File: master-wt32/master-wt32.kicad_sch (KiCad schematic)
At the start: 4 parts, among them J1 Conn_01x06_Male, J2 Conn_01x06_Male, J3 Conn_01x06_Female, J4 Conn_01x06_Female

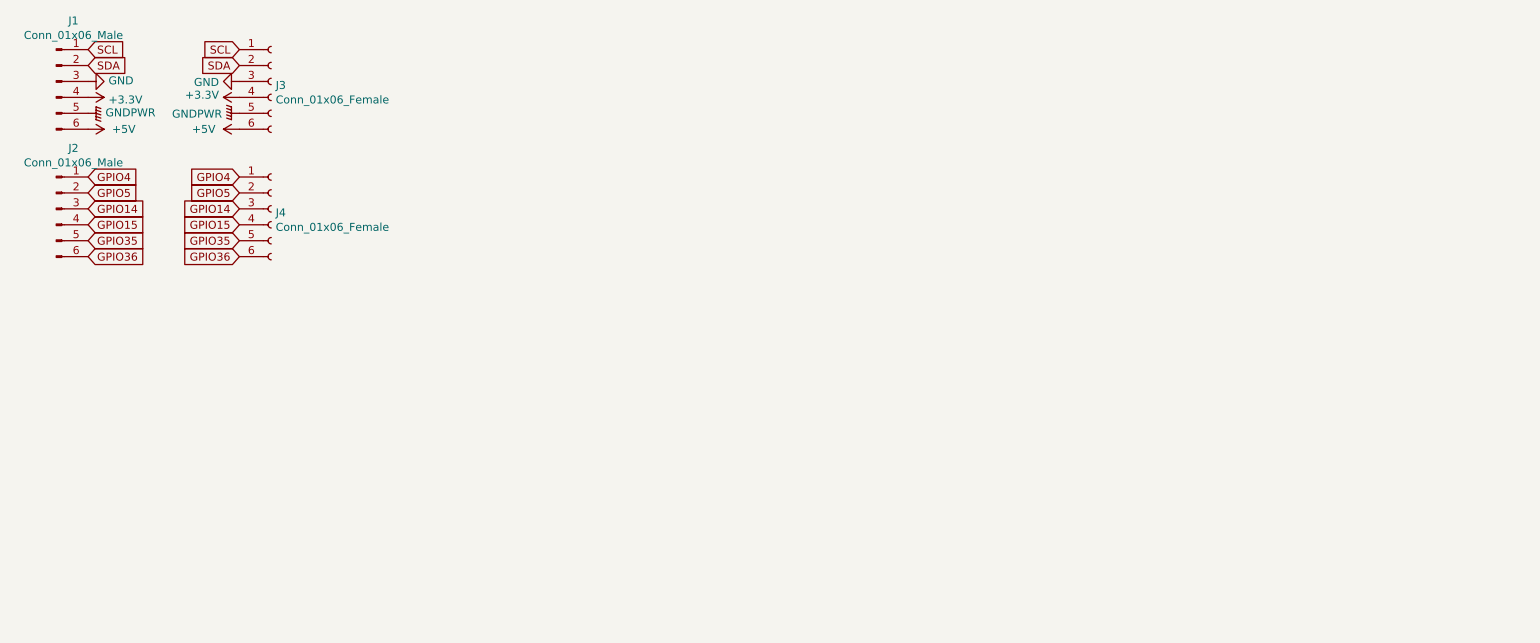
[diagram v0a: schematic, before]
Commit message: add components to master-wt32
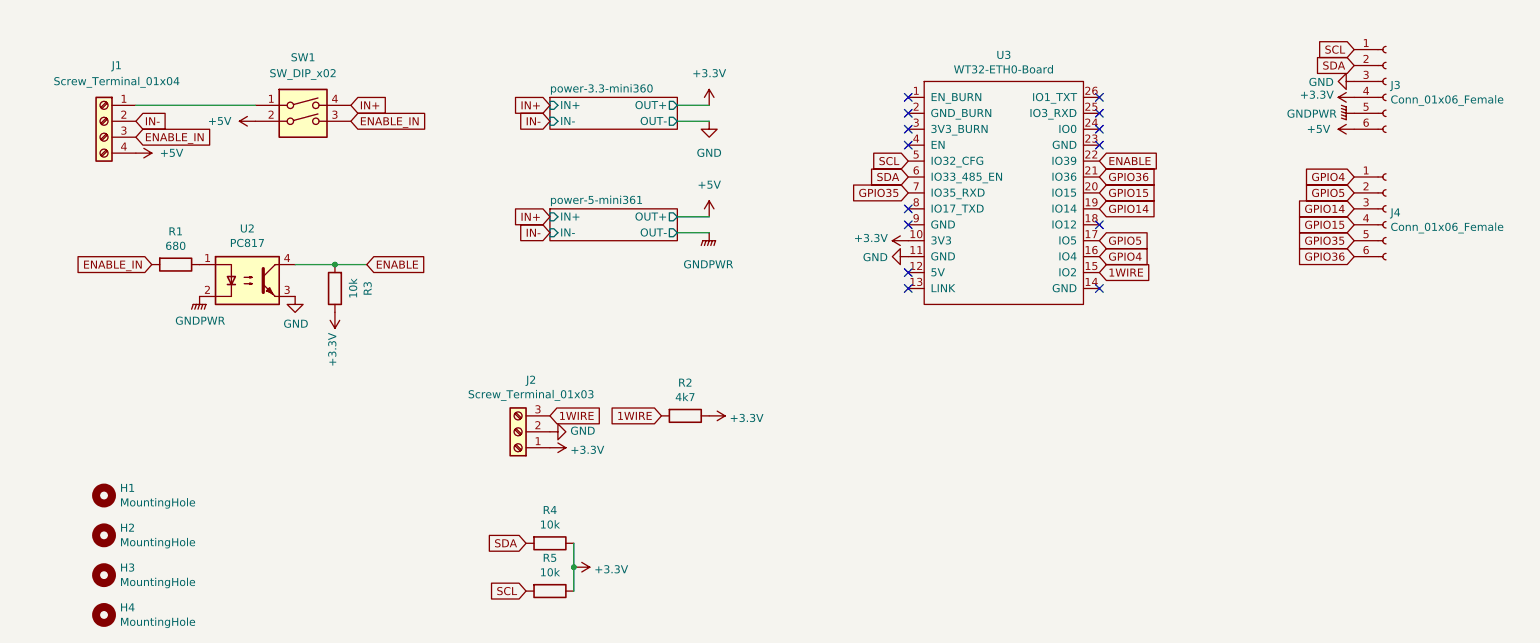
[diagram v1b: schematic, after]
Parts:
- removed J1, J2: Conn_01x06_Male, Connector_PinHeader_2.54mm:PinHeader_1x06_P2.54mm_Horizontal, symbol Connector:Conn_01x06_Male
- added H1, H2, H3, H4: MountingHole, MountingHole:MountingHole_3.2mm_M3, symbol Mechanical:MountingHole
- added J1: Screw_Terminal_01x04, TerminalBlock:TerminalBlock_bornier-4_P5.08mm, symbol Connector:Screw_Terminal_01x04
- added J2: Screw_Terminal_01x03, TerminalBlock:TerminalBlock_bornier-3_P5.08mm, symbol Connector:Screw_Terminal_01x03
- added R1: 680, Resistor_THT:R_Axial_DIN0207_L6.3mm_D2.5mm_P7.62mm_Horizontal, symbol Device:R
- added R2: 4k7, Resistor_THT:R_Axial_DIN0207_L6.3mm_D2.5mm_P7.62mm_Horizontal, symbol Device:R
- added R3, R4, R5: 10k, Resistor_THT:R_Axial_DIN0207_L6.3mm_D2.5mm_P7.62mm_Horizontal, symbol Device:R
- added SW1: SW_DIP_x02, Button_Switch_THT:SW_DIP_SPSTx02_Slide_9.78x7.26mm_W7.62mm_P2.54mm, symbol Switch:SW_DIP_x02
- added U2: PC817, Package_DIP:DIP-4_W7.62mm, symbol Isolator:PC817
- added U3: WT32-ETH0-Board, boards:WT32-ETH01-Board-Reversed, symbol master-wt32-eth01-rescue:WT32-ETH0-Board-boards
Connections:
- net +3V3: now also J2.1 (Pin_1), R2.1, R3.1, R4.1, R5.1, U3.10 (3V3)
- net +5V: now also J1.4 (Pin_4), SW1.2
- net GND: now also J2.2 (Pin_2), U2.3, U3.11 (GND)
- net GNDPWR: now also U2.2
- net GPIO14: now also U3.19 (IO14)
- net GPIO15: now also U3.20 (IO15)
- net GPIO35: now also U3.7 (IO35_RXD)
- net GPIO36: now also U3.21 (IO36)
- net GPIO4: now also U3.16 (IO4)
- net GPIO5: now also U3.17 (IO5)
- net SCL: now also R5.2, U3.5 (IO32_CFG)
- net SDA: now also R4.2, U3.6 (IO33_485_EN)
- new net: R1.1, U2.1
- new net: J1.1 (Pin_1), SW1.1
- new net 1WIRE: J2.3 (Pin_3), R2.2, U3.15 (IO2)
- new net ENABLE: R3.2, U2.4, U3.22 (IO39)
- new net ENABLE_IN: J1.3 (Pin_3), R1.2, SW1.3
- new net IN+: SW1.4
- new net IN-: J1.2 (Pin_2)
- no-connect marks 0 -> 14
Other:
- added sheet power-3.3-mini360 (../include/power-mini360.kicad_sch)
- added sheet power-5-mini361 (../include/power-mini360.kicad_sch)
- moved on the sheet: J3, J4

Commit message: route master-wt32
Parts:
- added D3, D4: LED, LED_THT:LED_D5.0mm, symbol Device:LED
- added R6: 330, Resistor_THT:R_Axial_DIN0207_L6.3mm_D2.5mm_P7.62mm_Horizontal, symbol Device:R
- added R7: 680, Resistor_THT:R_Axial_DIN0207_L6.3mm_D2.5mm_P7.62mm_Horizontal, symbol Device:R
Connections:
- net +3V3: now also R6.2
- net +5V: now also R7.2
- net GND: now also D3.2 (A)
- net GNDPWR: now also D4.2 (A)
- new net: D4.1 (K), R7.1
- new net: D3.1 (K), R6.1

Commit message: refactor master-wt32 pcb
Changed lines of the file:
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@@
     (in_bom yes) (on_board yes)
     (property "Reference" "H1" (id 0) (at 33.02 91.5416 0)
-      (effects (font (size 1.27 1.27)) (justify left))
+      (effects (font (size 1.27 1.27)) (justify left) hide)
     )
     (property "Value" "MountingHole" (id 1) (at 33.02 93.853 0)
@@
     (in_bom yes) (on_board yes)
     (property "Reference" "H2" (id 0) (at 33.02 97.8916 0)
-      (effects (font (size 1.27 1.27)) (justify left))
+      (effects (font (size 1.27 1.27)) (justify left) hide)
     )
     (property "Value" "MountingHole" (id 1) (at 33.02 100.203 0)
@@
     (in_bom yes) (on_board yes)
     (property "Reference" "H3" (id 0) (at 33.02 104.2416 0)
-      (effects (font (size 1.27 1.27)) (justify left))
+      (effects (font (size 1.27 1.27)) (justify left) hide)
     )
     (property "Value" "MountingHole" (id 1) (at 33.02 106.553 0)
@@
     (in_bom yes) (on_board yes)
     (property "Reference" "H4" (id 0) (at 33.02 110.5916 0)
-      (effects (font (size 1.27 1.27)) (justify left))
+      (effects (font (size 1.27 1.27)) (justify left) hide)
     )
     (property "Value" "MountingHole" (id 1) (at 33.02 112.903 0)

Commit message: refactor master-wt32
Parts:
- removed D3: LED, LED_THT:LED_D5.0mm, symbol Device:LED
- removed R6: 330, Resistor_THT:R_Axial_DIN0207_L6.3mm_D2.5mm_P7.62mm_Horizontal, symbol Device:R
- removed SW1: SW_DIP_x02, Button_Switch_THT:SW_DIP_SPSTx02_Slide_9.78x7.26mm_W7.62mm_P2.54mm, symbol Switch:SW_DIP_x02
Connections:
- net +3V3: no longer U3.10 (3V3)
- net +5V: now also U3.12 (5V)
- net IN+: now also J1.1 (Pin_1)
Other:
- removed sheet power-3.3-mini360
- removed sheet power-5-mini361
- added sheet power-5-lm2596 (../include/power-lm2596.kicad_sch)
- added sheet regulator-3.3 (../include/regulator-3.3.kicad_sch)
- moved on the sheet: D4, R7
